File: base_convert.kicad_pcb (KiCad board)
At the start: 2 copper layers, 93.3 x 100 mm, 124 parts, among them J1 ISP, J3 Vin, Q1 Q_PMOS_GSD, Q10 Q_PNP_BEC, Q11 Q_PNP_BEC, Q12 Q_PNP_BEC, Q13 Q_PNP_BEC, Q14 Q_PNP_BEC, Q15 Q_PNP_BEC, Q16 Q_PNP_BEC, Q17 Q_PNP_BEC, Q18 Q_PNP_BEC, Q19 Q_PNP_BEC, Q2 Q_PNP_BEC, Q20 Q_NPN_BEC, Q21 Q_NPN_BEC, Q22 Q_NPN_BEC, Q23 Q_NPN_BEC, Q24 Q_NPN_BEC, Q25 Q_NPN_BEC, Q26 Q_NPN_BEC, Q27 Q_NPN_BEC, Q3 Q_PNP_BEC, Q4 Q_PNP_BEC, Q5 Q_PNP_BEC, Q6 Q_NPN_BEC, Q7 Q_NPN_BEC, Q8 Q_NPN_BEC, Q9 Q_NPN_BEC, SW1 SELECT, SW10 1, SW11 4, SW12 7, SW13 A, SW14 CLEAR, SW15 B, SW16 C, SW17 D, SW18 E, SW2 3, SW3 6, SW4 9, SW5 F, SW6 2, SW7 5, SW8 8, SW9 0, U1 MIC5317-3.3YM5-TR, U2 MSP430FR2033IPMR

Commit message: switch resitors to arrays
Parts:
- removed R10, R25, R26, R27, R28, R29, R30, R31, R32, R7, R8, R9: 150, Resistors_SMD:R_0603
- removed R11, R12, R13, R14, R15, R16, R17, R18, R19, R20, R21, R22, R23, R24, R3, R33, R34, R35, R36, R37, R38, R39, R4, R40, R5, R6: 4.7k, Resistors_SMD:R_0603
- added RN1: 4.7k, Resistors_SMD:R_Array_Convex_4x1206, F.Cu at (-53.7, 77.8)
- added RN10: 4.7k, Resistors_SMD:R_Array_Convex_4x1206, F.Cu at (-99.0, 138.4)
- added RN2: 150, Resistors_SMD:R_Array_Convex_4x1206, F.Cu at (68.8, 79.2)
- added RN3: 4.7k, Resistors_SMD:R_Array_Convex_4x1206, F.Cu at (-30.5, 54.8)
- added RN4: 4.7k, Resistors_SMD:R_Array_Convex_4x1206, F.Cu at (-79.1, 81.8)
- added RN5: 4.7k, Resistors_SMD:R_Array_Convex_4x1206, F.Cu at (-76.2, 104.9)
- added RN6: 4.7k, Resistors_SMD:R_Array_Convex_4x1206, F.Cu at (-70.8, 124.6)
- added RN7: 150, Resistors_SMD:R_Array_Convex_4x1206, F.Cu at (-83.4, 109.7)
- added RN8: 150, Resistors_SMD:R_Array_Convex_4x1206, F.Cu at (-81.0, 135.9)
- added RN9: 4.7k, Resistors_SMD:R_Array_Convex_4x1206, F.Cu at (-100.3, 108.9)
- moved Q3 277.6 mm to (-46.2, 78.3)
- moved Q24 270.5 mm to (-89.9, 125.4)
- moved Q4 268.6 mm to (-46.0, 84.1)
- moved Q20 268.6 mm to (-89.7, 102.6)
- moved Q5 268.4 mm to (-45.7, 89.7)
- moved Q27 265.4 mm to (-91.0, 143.2)
- moved Q12 262.9 mm to (-66.0, 84.3)
- moved Q2 262.9 mm to (-46.0, 71.2)
- moved Q16 262.3 mm to (-65.5, 108.5)
- moved Q25 262.1 mm to (-90.6, 130.8)
- moved Q22 259.5 mm to (-89.6, 113.6)
- moved Q11 255.4 mm to (-66.5, 78.5)
- moved Q14 253.9 mm to (-65.8, 96.3)
- moved Q21 253.1 mm to (-89.7, 108.0)
- moved Q17 252.7 mm to (-64.0, 115.6)
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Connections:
- JP1 pad 2: VCC -> +3V3
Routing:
- net VCC: track 11.6 -> 157.5 mm
- net /Keypad/CLEAR: track 0.00 -> 58.1 mm, vias 0 -> 2
- net /Keypad/ROW1: track 97.8 -> 69.7 mm, vias 0 -> 3
- net +3V3: track 0.00 -> 19.0 mm
- net /Keypad/ROW0: track 43.5 -> 60.9 mm, vias 0 -> 2
- net /Keypad/ROW2: track 95.3 -> 79.3 mm, vias 0 -> 3
- net GND: track 0.00 -> 13.1 mm, vias 0 -> 6
- net /SBWTCK: track 0.00 -> 12.2 mm, vias 0 -> 2
- net /BATT_V: track 0.00 -> 12.1 mm
- net Net-(J1-Pad1): track 0.00 -> 10.7 mm
- net /SBWTDIO: track 0.00 -> 9.38 mm, vias 0 -> 2
- net /Keypad/COL2: track 61.1 -> 65.1 mm, vias 5 -> 4
- net /Keypad/COL0: track 118.5 -> 115.0 mm, vias 4 -> 7
- net /Keypad/ROW3: track 90.5 -> 88.3 mm
- net /Keypad/COL3: track 47.1 -> 48.3 mm
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- added copper zone on B.Cu, net GND

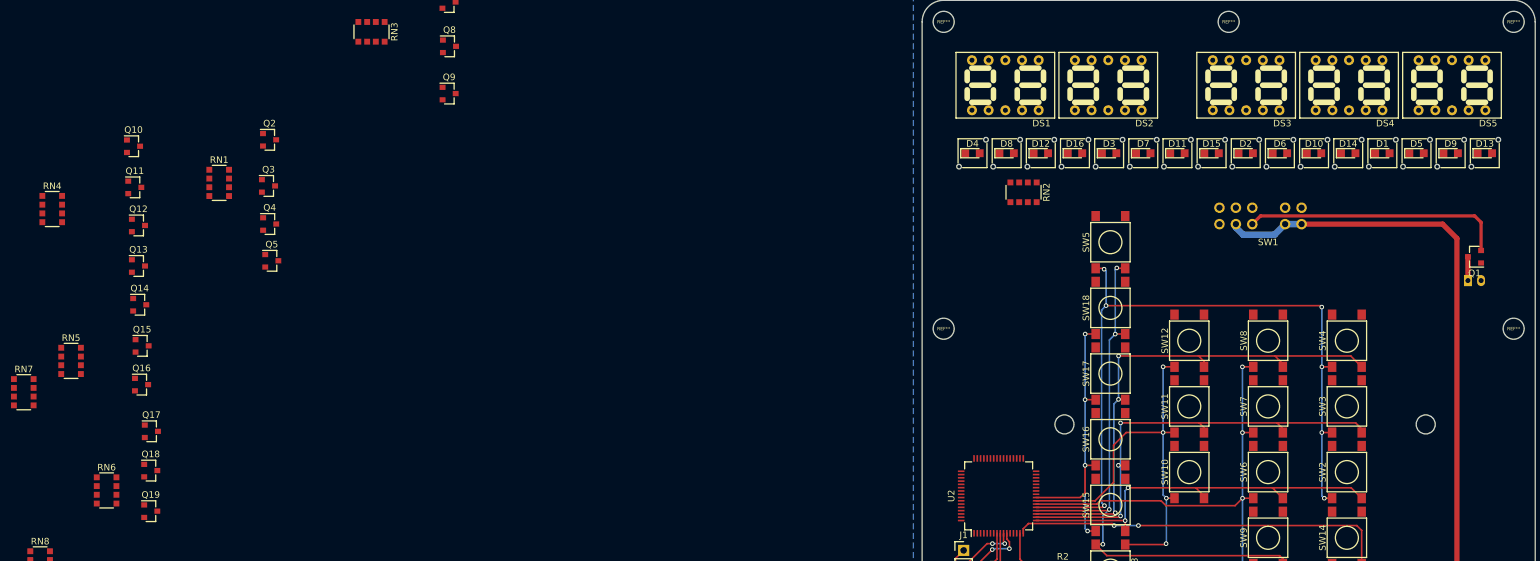
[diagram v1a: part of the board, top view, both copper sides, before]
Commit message: start tran layout
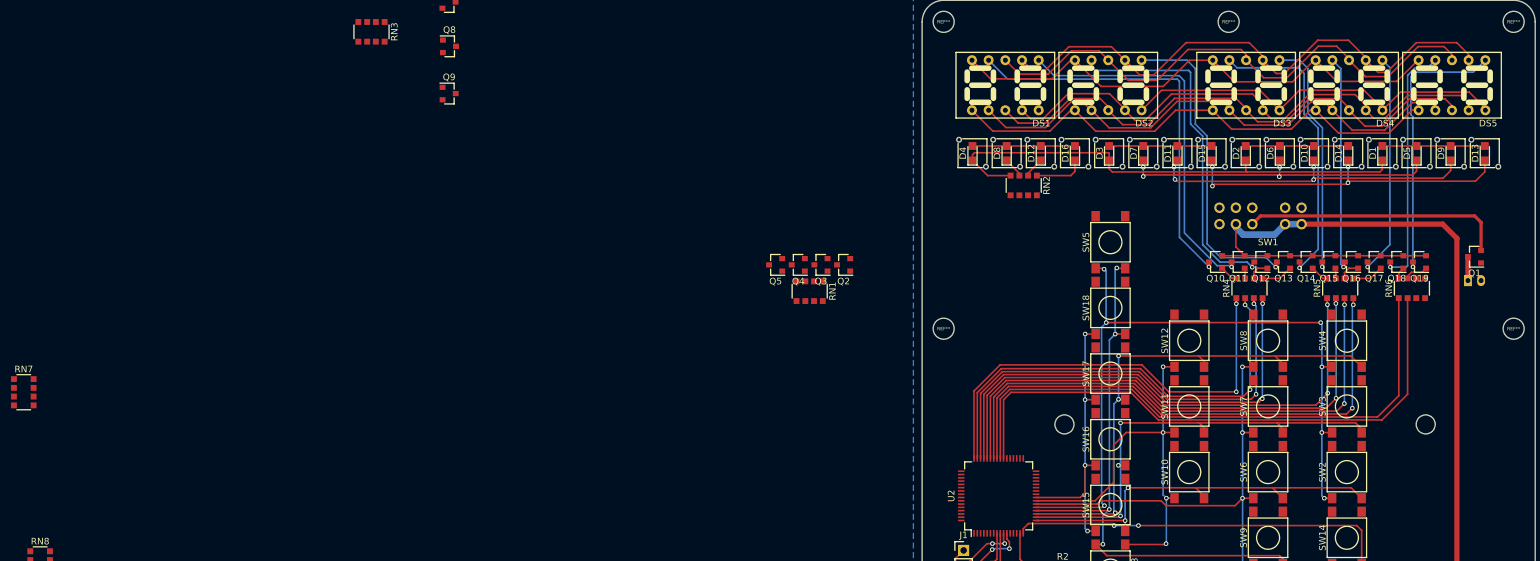
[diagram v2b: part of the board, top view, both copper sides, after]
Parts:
- moved RN6 201.1 mm to (127.9, 93.8), turned to 90 degrees
- moved Q19 196.9 mm to (129.1, 89.8), turned to 180 degrees
- moved RN5 193.5 mm to (117.0, 93.8), turned to 90 degrees
- moved Q18 192.4 mm to (125.6, 89.8), turned to 180 degrees
- moved Q17 187.9 mm to (122.2, 89.8), turned to 180 degrees
- moved Q16 185.2 mm to (118.7, 89.8), turned to 180 degrees
- moved RN4 182.7 mm to (103.2, 93.8), turned to 90 degrees
- moved Q15 181.1 mm to (115.2, 89.8), turned to 180 degrees
- moved Q14 177.7 mm to (111.8, 89.8), turned to 180 degrees
- moved Q13 174.3 mm to (108.3, 89.8), turned to 180 degrees
- moved Q12 171.0 mm to (104.9, 89.8), turned to 180 degrees
- moved Q11 168.4 mm to (101.5, 89.8), turned to 180 degrees
- moved Q10 165.7 mm to (98.0, 89.8), turned to 180 degrees
- moved RN1 91.4 mm to (36.2, 94.3), turned to 270 degrees
- moved Q2 89.4 mm to (41.4, 90.3), turned to 180 degrees
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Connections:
- RN1 pad 1: /Binary Display/NIBBLE0 -> Net-(Q2-Pad1)
- RN1 pad 2: /Binary Display/NIBBLE1 -> Net-(Q3-Pad1)
- RN1 pad 3: /Binary Display/NIBBLE2 -> Net-(Q4-Pad1)
- RN1 pad 4: /Binary Display/NIBBLE3 -> Net-(Q5-Pad1)
- RN1 pad 5: Net-(Q5-Pad1) -> /Binary Display/NIBBLE3
- RN1 pad 6: Net-(Q4-Pad1) -> /Binary Display/NIBBLE2
- RN1 pad 7: Net-(Q3-Pad1) -> /Binary Display/NIBBLE1
- RN1 pad 8: Net-(Q2-Pad1) -> /Binary Display/NIBBLE0
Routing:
- net /7 Segment Displays/~DIGIT9: track 0.00 -> 88.9 mm
- net /7 Segment Displays/~DIGIT8: track 0.00 -> 88.3 mm
- net /7 Segment Displays/A: track 0.00 -> 84.6 mm
- net /7 Segment Displays/B: track 0.00 -> 83.8 mm
- net /7 Segment Displays/~DIGIT7: track 0.00 -> 83.0 mm, vias 0 -> 2
- net /7 Segment Displays/G: track 0.00 -> 82.1 mm
- net /7 Segment Displays/~DIGIT6: track 0.00 -> 81.9 mm, vias 0 -> 2
- net /7 Segment Displays/C: track 0.00 -> 81.8 mm
- net /7 Segment Displays/D: track 0.00 -> 81.4 mm
- net /7 Segment Displays/~DIGIT5: track 0.00 -> 80.7 mm, vias 0 -> 2
- net /7 Segment Displays/~DIGIT4: track 0.00 -> 79.6 mm, vias 0 -> 2
- net /7 Segment Displays/F: track 0.00 -> 79.1 mm
- net /7 Segment Displays/E: track 0.00 -> 78.5 mm
- net /Binary Display/BIT3: track 0.00 -> 76.1 mm
- net /7 Segment Displays/~DIGIT3: track 0.00 -> 70.7 mm, vias 0 -> 2
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
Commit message: layout complete, requires cleanup
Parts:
- moved RN10 175.1 mm to (69.5, 90.7), turned to 270 degrees
- moved RN9 168.2 mm to (67.7, 101.7), turned to 270 degrees
- moved Q24 165.1 mm to (70.6, 86.7), turned to 180 degrees
- moved Q25 163.8 mm to (67.2, 86.7), turned to 180 degrees
- moved Q20 162.7 mm to (72.9, 97.7), turned to 180 degrees
- moved Q26 162.5 mm to (63.7, 86.7), turned to 180 degrees
- moved Q27 161.5 mm to (60.2, 86.7), turned to 180 degrees
- moved Q21 159.5 mm to (69.5, 97.7), turned to 180 degrees
- moved Q22 156.4 mm to (66.0, 97.7), turned to 180 degrees
- moved Q23 153.8 mm to (62.5, 97.7), turned to 180 degrees
- moved RN8 152.2 mm to (61.4, 82.2), turned to 270 degrees
- moved RN7 148.0 mm to (63.7, 93.7), turned to 270 degrees
- moved RN3 110.5 mm to (75.5, 86.2)
- moved Q6 101.7 mm to (76.6, 82.2), turned to 180 degrees
- moved Q7 97.2 mm to (73.2, 82.2), turned to 180 degrees
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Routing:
- net /HEX_INPUT: track 0.00 -> 89.6 mm, vias 0 -> 1
- net /BIN_INPUT: track 0.00 -> 85.9 mm, vias 0 -> 1
- net /DEC_INPUT: track 0.00 -> 84.2 mm, vias 0 -> 1
- net /Binary Display/NIBBLE0: track 0.00 -> 74.3 mm, vias 0 -> 2
- net /Binary Display/NIBBLE1: track 0.00 -> 72.6 mm, vias 0 -> 2
- net /Binary Display/NIBBLE2: track 0.00 -> 68.8 mm, vias 0 -> 2
- net /Binary Display/NIBBLE3: track 0.00 -> 67.0 mm, vias 0 -> 2
- net /Binary Display/LED_BIT0: track 0.00 -> 55.2 mm, vias 0 -> 2
- net /7 Segment Displays/A: track 84.6 -> 138.6 mm
- net /Binary Display/LED_BIT1: track 0.00 -> 53.8 mm, vias 0 -> 2
- net /7 Segment Displays/B: track 83.8 -> 136.6 mm, vias 0 -> 1
- net /Binary Display/LED_BIT2: track 0.00 -> 52.4 mm, vias 0 -> 2
- net /Binary Display/LED_BIT3: track 0.00 -> 51.2 mm, vias 0 -> 2
- net /7 Segment Displays/DP: track 60.0 -> 105.7 mm, vias 0 -> 1
- net /7 Segment Displays/C: track 81.8 -> 124.7 mm, vias 0 -> 1
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
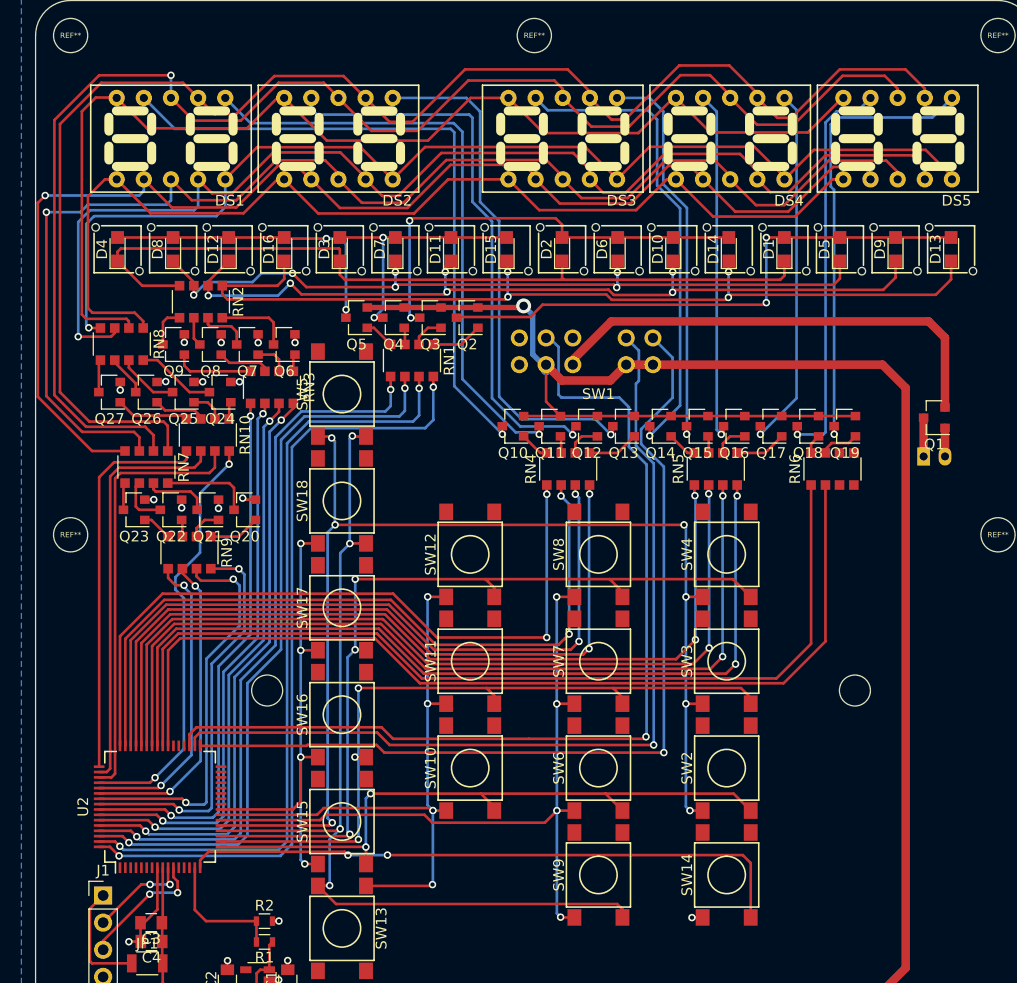
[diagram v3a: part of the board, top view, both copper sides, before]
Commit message: traces cleaned up
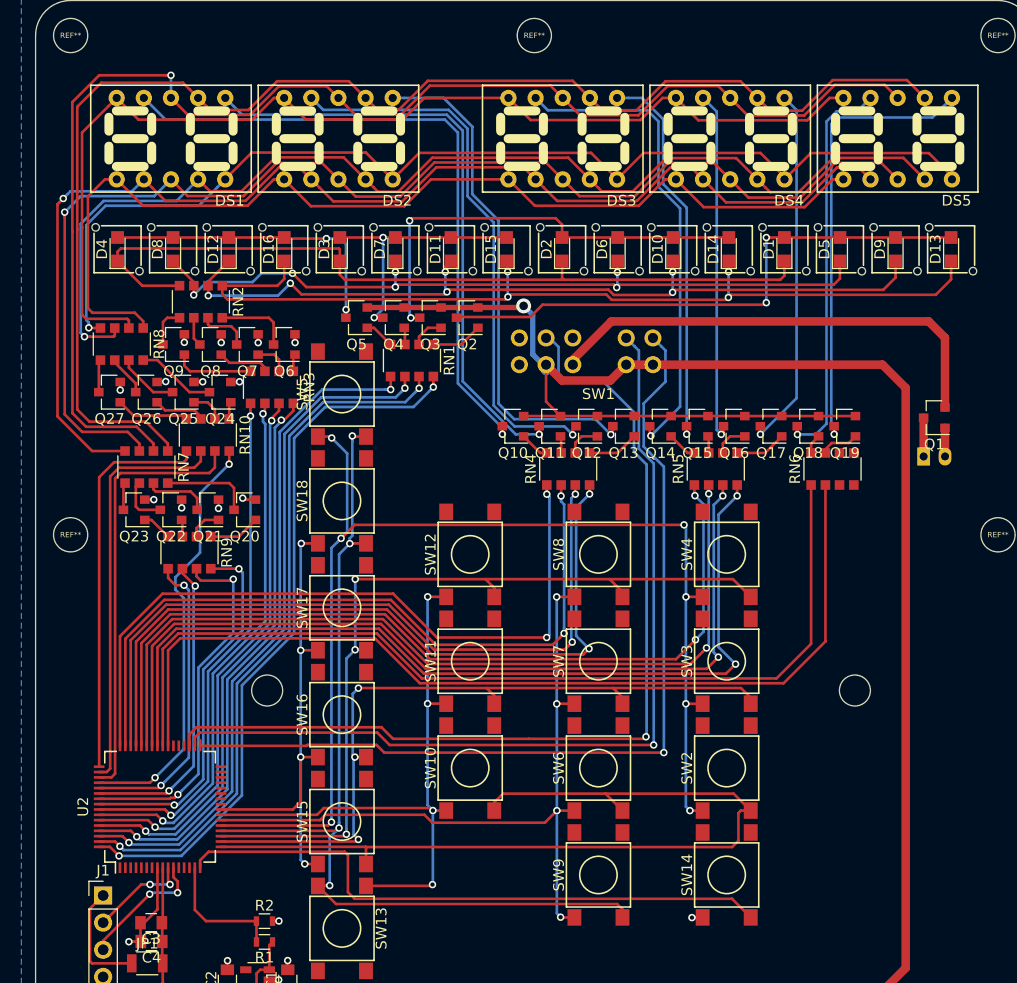
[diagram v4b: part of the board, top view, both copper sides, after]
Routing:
- net /Keypad/ROW0: track 60.9 -> 82.1 mm, vias 2 -> 0
- net /7 Segment Displays/A: track 138.6 -> 129.3 mm
- net /7 Segment Displays/B: track 136.6 -> 128.0 mm
- net /7 Segment Displays/C: track 124.7 -> 117.4 mm
- net /Binary Display/NIBBLE0: track 74.3 -> 67.5 mm
- net /Binary Display/NIBBLE1: track 72.6 -> 66.0 mm
- net /7 Segment Displays/D: track 121.5 -> 115.2 mm
- net /7 Segment Displays/G: track 111.2 -> 105.5 mm
- net /7 Segment Displays/F: track 107.2 -> 101.7 mm
- net /Binary Display/NIBBLE2: track 68.8 -> 64.4 mm
- net /Binary Display/NIBBLE3: track 67.0 -> 63.0 mm
- net /7 Segment Displays/DP: track 105.7 -> 102.5 mm
- net /7 Segment Displays/SEG-B: track 37.2 -> 34.2 mm
- net /Binary Display/LED_BIT0: track 55.2 -> 52.5 mm
- net /7 Segment Displays/SEG-A: track 37.4 -> 34.8 mm
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
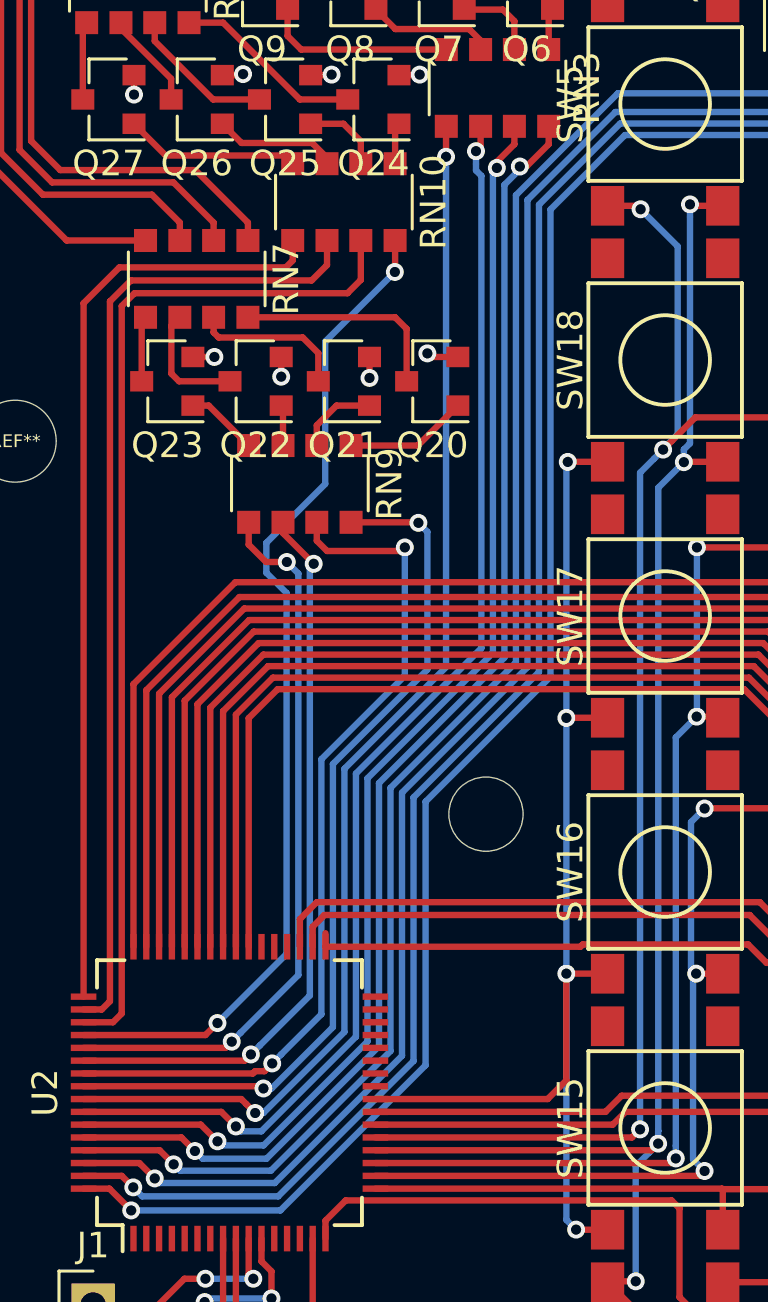
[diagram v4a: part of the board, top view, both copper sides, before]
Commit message: add JST connector 3d model
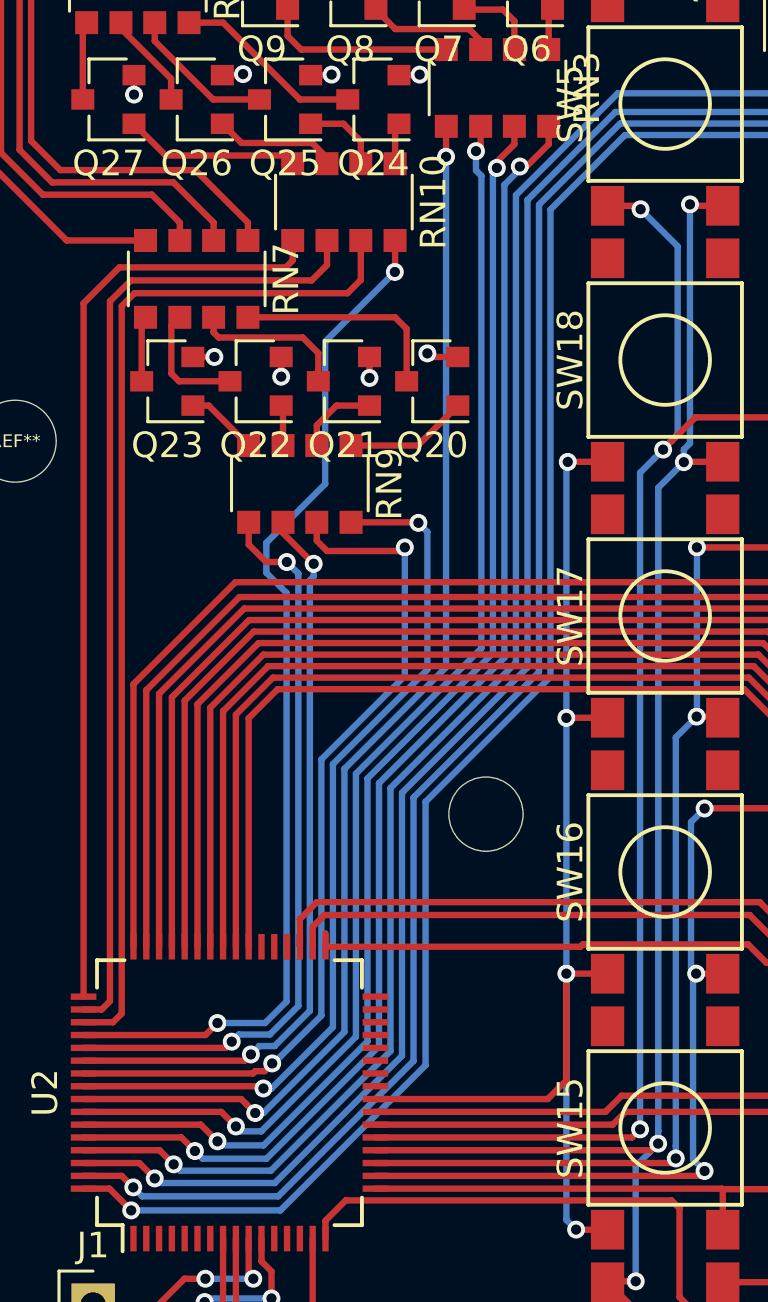
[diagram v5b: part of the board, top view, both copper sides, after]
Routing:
- net /7 Segment Displays/SEG-E: track 39.5 -> 40.6 mm
- net /7 Segment Displays/SEG-D: track 28.5 -> 29.2 mm
